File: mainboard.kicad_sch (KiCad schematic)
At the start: 39 parts, among them J1 DRV8833-1, J10 Conn_02x04_Counter_Clockwise, J11 Conn_02x04_Counter_Clockwise, J12 Conn_02x04_Counter_Clockwise, J2 DRV8833-0, J3 Conn_01x02, J4 Screw_Terminal_01x06, J5 Screw_Terminal_01x06, J6 VIM4_HEADER, J7 Conn_01x02, J8 Conn_01x02, J9 Conn_02x04_Counter_Clockwise, Q1 2N7000, Q2 2N7000, SW1 RotaryEncoder_Switch, U1 MCP23017_SP

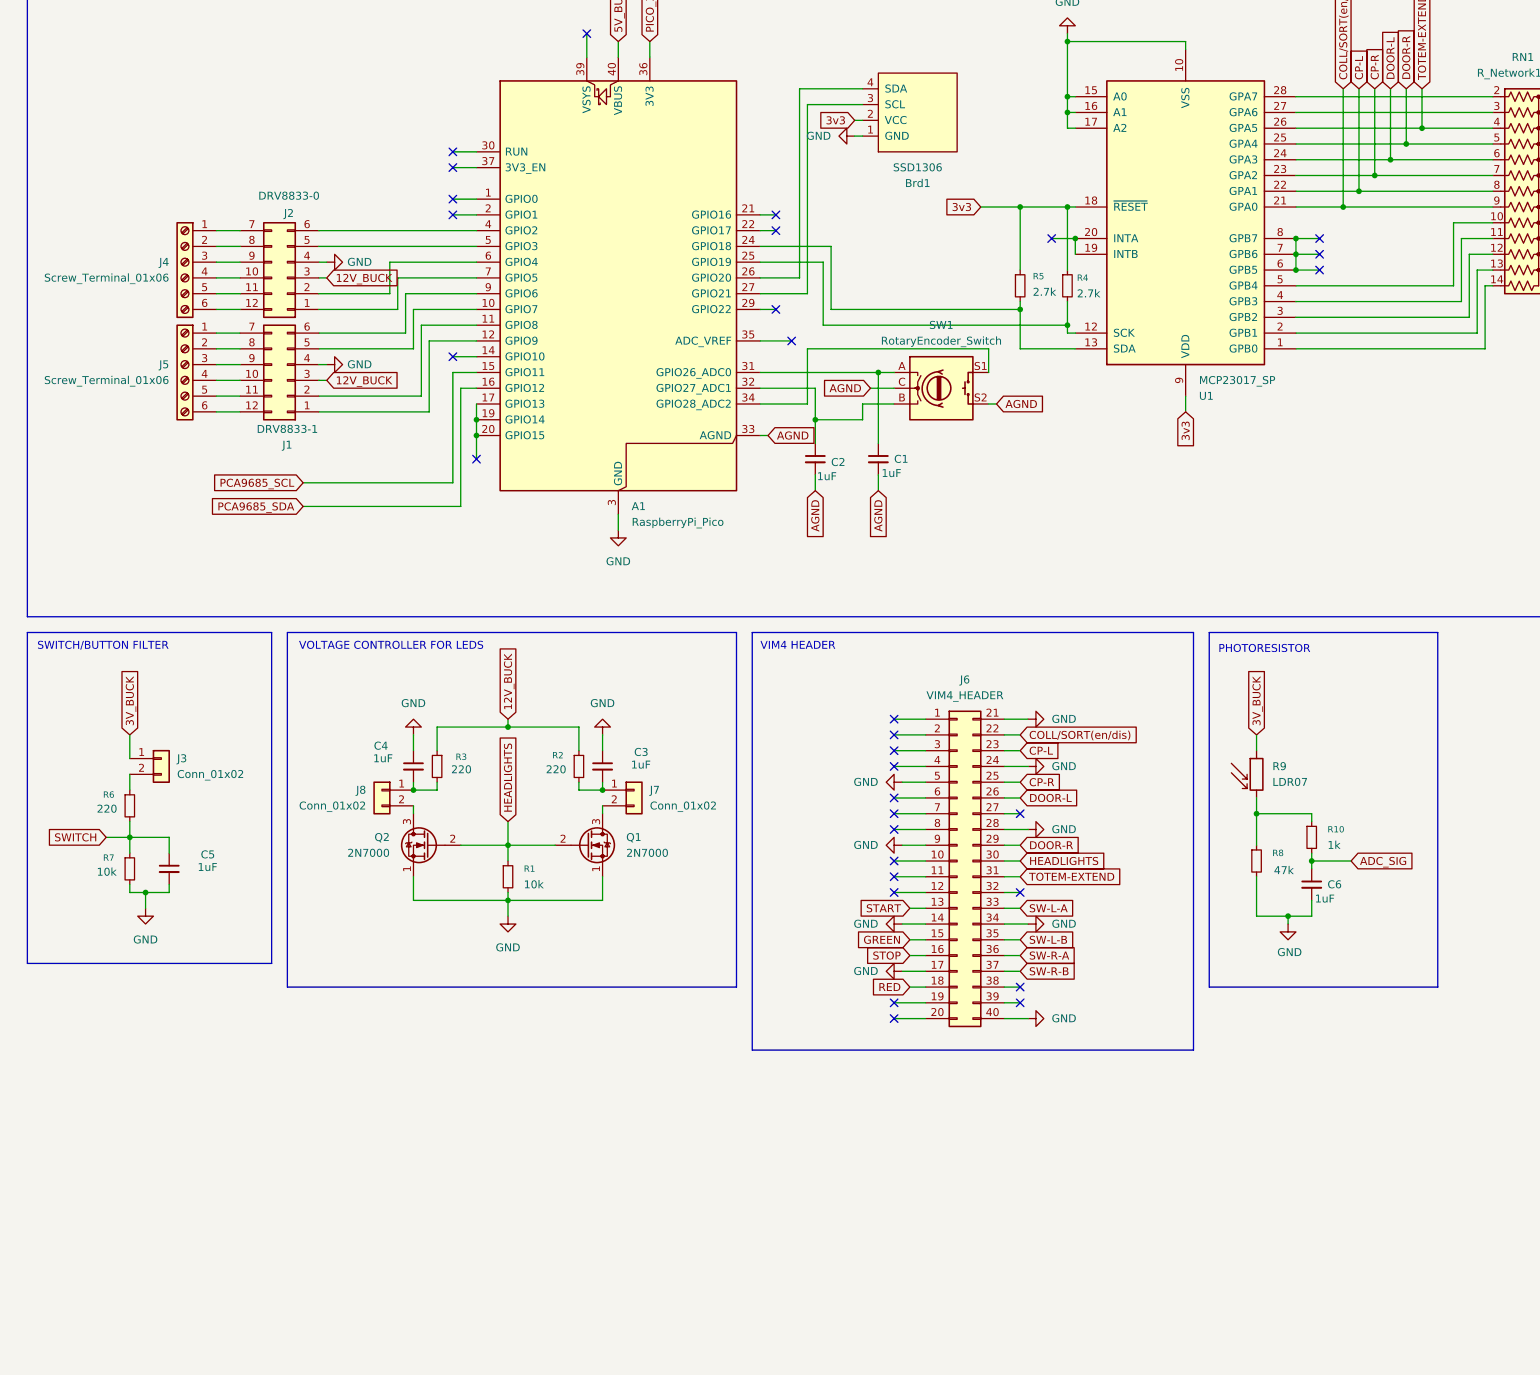
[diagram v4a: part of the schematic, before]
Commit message: Circuit adjustments / PCB component Grouping
Removed resistor on LDR in schem. Changed to 10k resistor. Added hole distance for PCA9685, SSD1309.  Grouped components.  Awaiting PIC_FOR_ADC from Dustin
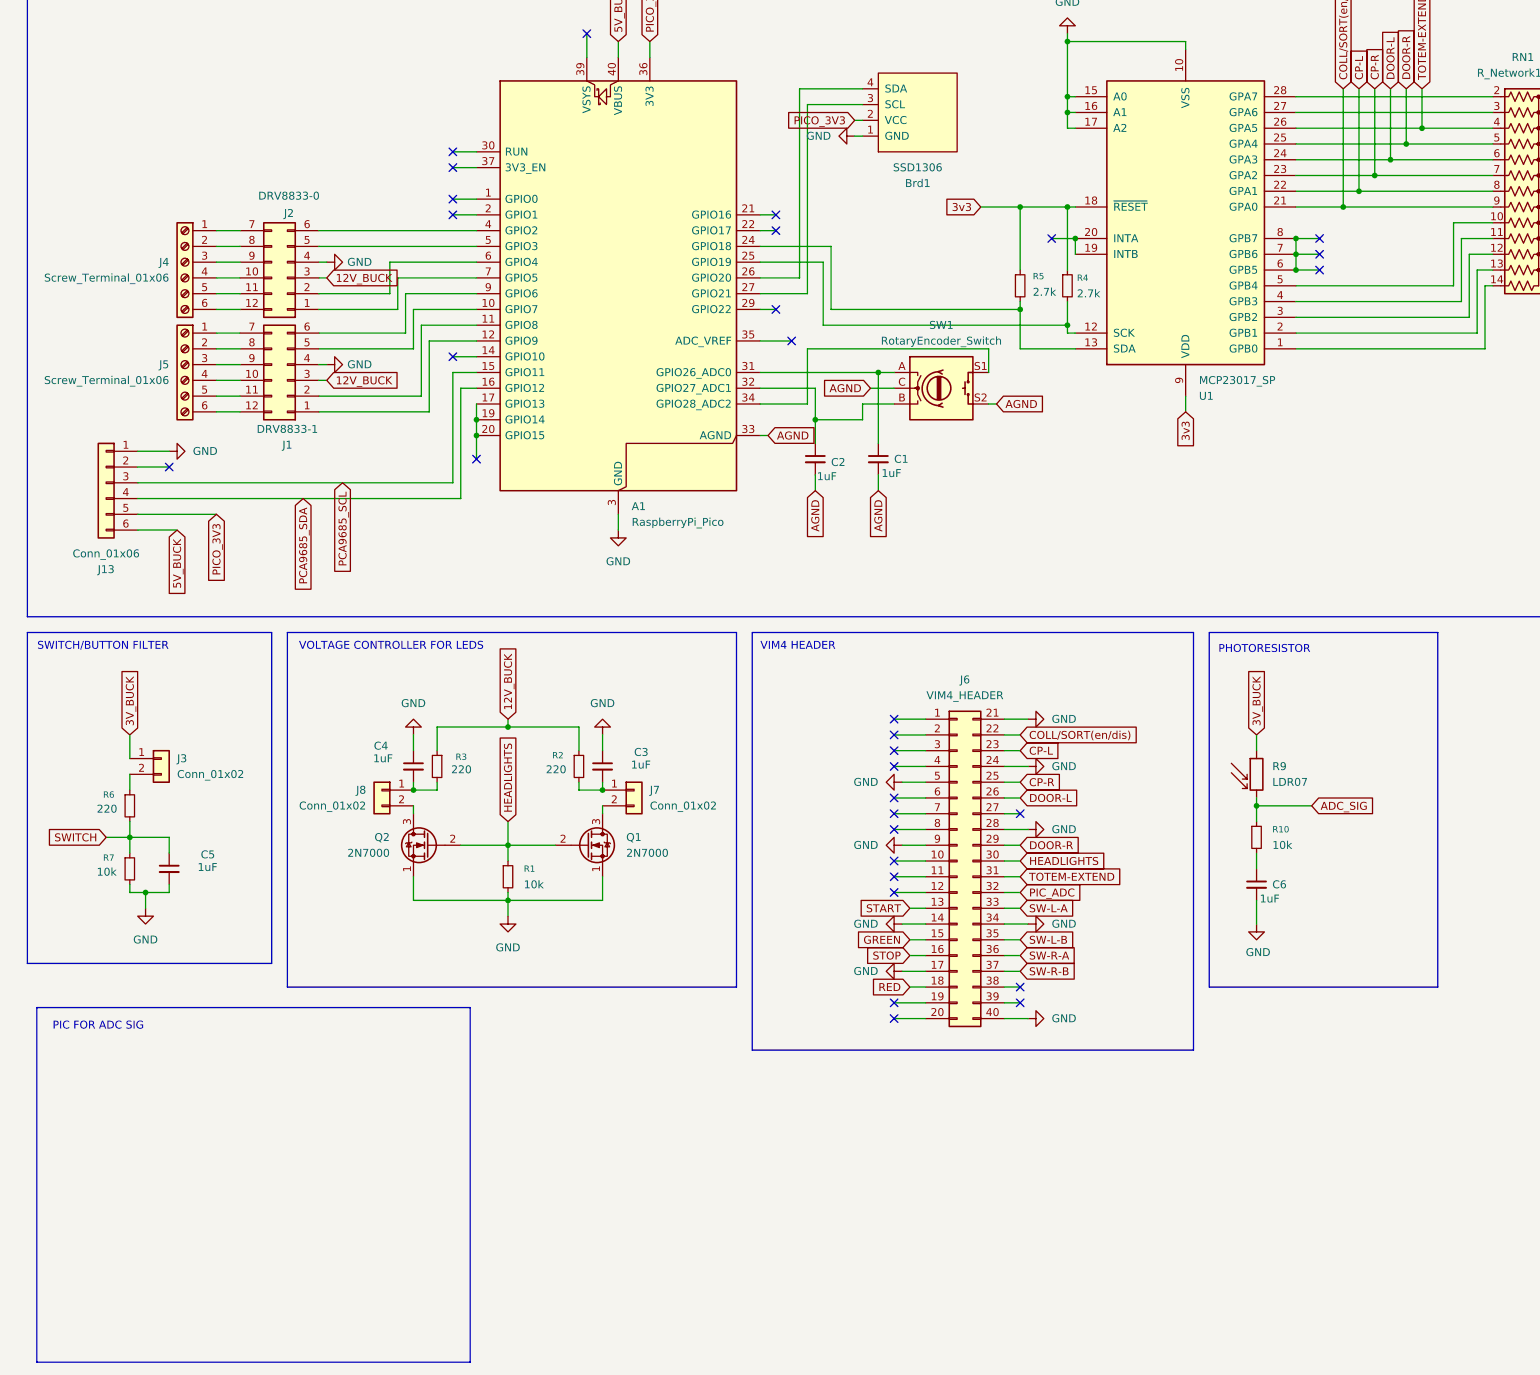
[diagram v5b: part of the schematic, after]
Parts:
- removed R8: 47k, Resistor_SMD:R_0805_2012Metric, symbol Device:R_Small
- added J13: Conn_01x06, Connector_JST:JST_EH_B6B-EH-A_1x06_P2.50mm_Vertical, symbol Connector_Generic:Conn_01x06
- R10: value 1k -> 10k
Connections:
- net 3v3: no longer Brd1.2 (VCC)
- net 5V_BUCK: now also J13.6 (Pin_6)
- net ADC_SIG: now also R10.1, R9.2; no longer C6.1, R10.2
- net GND: now also J13.1 (Pin_1)
- net PCA9685_SCL: now also J13.3 (Pin_3)
- net PCA9685_SDA: now also J13.4 (Pin_4)
- net PICO_3V3: now also Brd1.2 (VCC), J13.5 (Pin_5)
- net PIC_ADC: now reaches J6.32 (Pin_32)
- new net: C6.1, R10.2
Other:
- note added: "PIC FOR ADC SIG"
- moved on the sheet: C6, R10

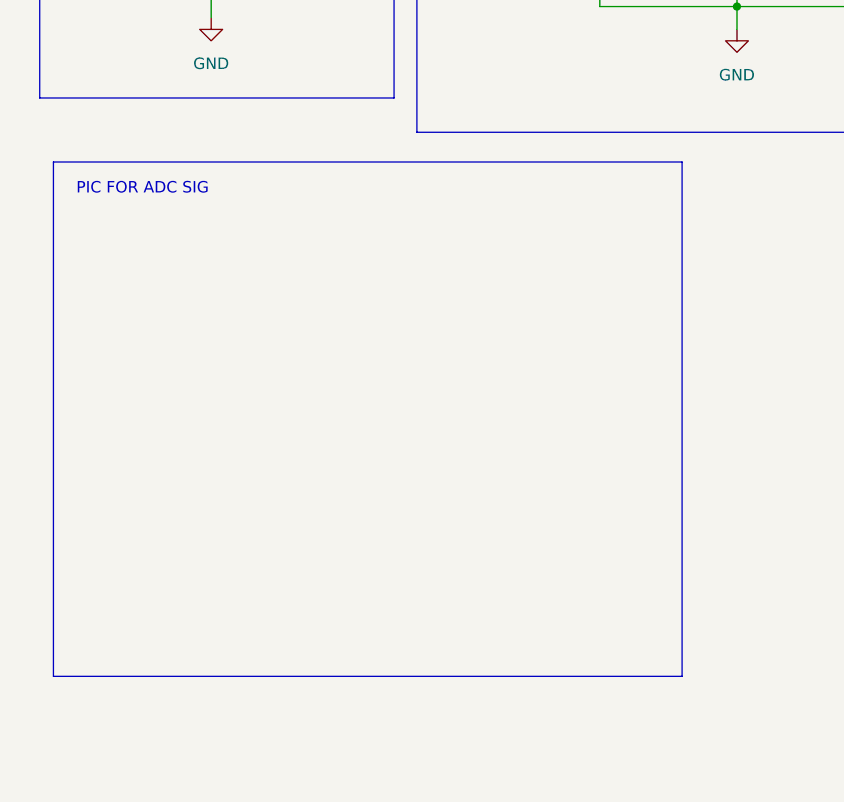
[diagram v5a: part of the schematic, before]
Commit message: PIC16F819-ISO Added
Added PIC, changed footprint to match our 18pin SMD.

LDR circuit and connection to VIM4 need to be made
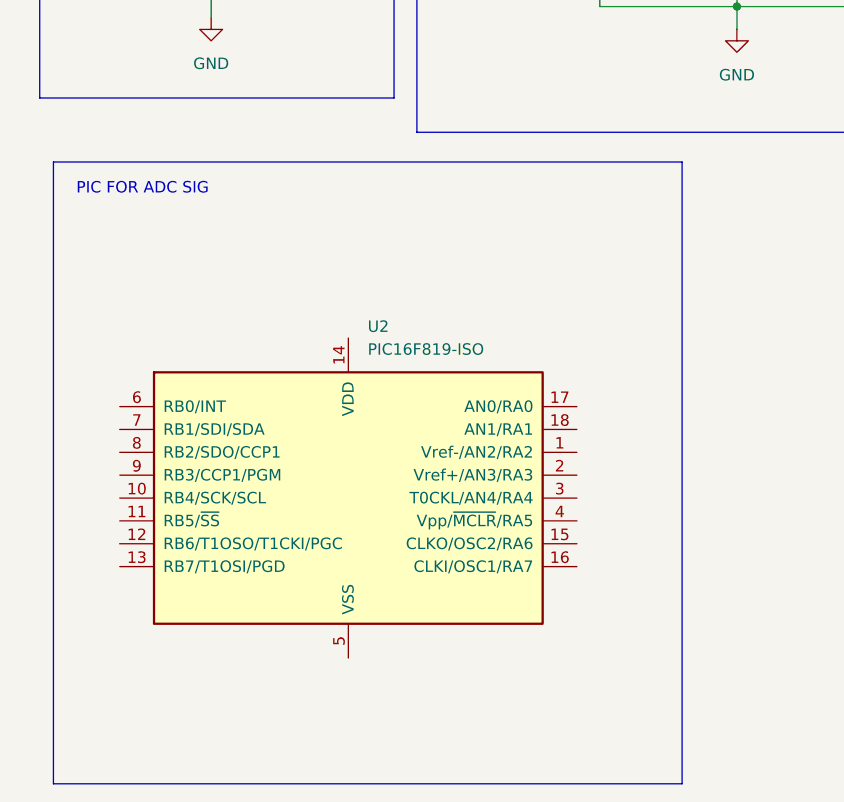
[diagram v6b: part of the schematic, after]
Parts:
- added U2: PIC16F819-ISO, Package_SO:SOIC-18W_7.5x11.6mm_P1.27mm, symbol MCU_Microchip_PIC16:PIC16F819-ISO
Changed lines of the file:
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@@
 	(rectangle
 		(start 14.224 188.722)
-		(end 84.074 245.872)
+		(end 84.074 257.81)
 		(stroke
 			(width 0)
@@
 					(unit 1)
 				)
+			)
+		)
+	)
+	(symbol
+		(lib_id "MCU_Microchip_PIC16:PIC16F819-ISO")
+		(at 46.99 226.06 0)
+		(unit 1)
+		(exclude_from_sim no)
+		(in_bom yes)
+		(on_board yes)
+		(dnp no)
+		(fields_autoplaced yes)
+		(property "Reference" "U2"
+			(at 49.1333 207.01 0)
+			(effects
+				(font
+					(size 1.27 1.27)
+				)
+				(justify left)
+			)
+		)
+		(property "Value" "PIC16F819-ISO"
+			(at 49.1333 209.55 0)
+			(effects
+				(font
+					(size 1.27 1.27)
+				)
+				(justify left)
+			)
+		)
+		(property "Footprint" "Package_SO:SOIC-18W_7.5x11.6mm_P1.27mm"
+			(at 46.99 226.06 0)
+			(effects
+				(font
+					(size 1.27 1.27)
+					(italic yes)
+				)
+				(hide yes)
+			)
+		)
+		(property "Datasheet" "http://ww1.microchip.com/downloads/en/DeviceDoc/39598F.pdf"
+			(at 46.99 226.06 0)
+			(effects
+				(font
+					(size 1.27 1.27)
+				)
+				(hide yes)
+			)
+		)
+		(property "Description" "PIC16F819, 3584B Flash, 256B SRAM, 256B EEPROM, ADC, SOIC18"
+			(at 46.99 226.06 0)
+			(effects
+				(font
+					(size 1.27 1.27)
+				)
+				(hide yes)
+			)
+		)
+		(pin "7"
+		)
+		(pin "8"
+		)
+		(pin "11"
+		)
+		(pin "6"
+		)
+		(pin "15"
+		)
+		(pin "9"
+		)
+		(pin "13"
+		)
+		(pin "17"
+		)
+		(pin "2"
+		)
+		(pin "3"
+		)
+		(pin "12"
+		)
+		(pin "14"
+		)
+		(pin "10"
+		)
+		(pin "5"
+		)
+		(pin "18"
+		)
+		(pin "1"
+		)
+		(pin "4"
+		)
+		(pin "16"
+		)
+		(instances
+			(project ""
+				(path "/c17272df-bb38-44d5-9de0-abe2e6f0941d"
+					(reference "U2")
+					(unit 1)
+				)

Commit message: Rearrangement and first pour
Modified the order of operations for terminal block to fuse to buck. Added a few things like the holes for the Roboclaws, removed the display, since we're going to wire it using a JST connector in order for it to exist somewhere else on the robot.  I added a PIC footprint that fits the PIC16F819-ISO, and generally hooked it up.

I still need to check with Dustin and make sure that the VIM4 connection to the PIC is the one we want to use.

I also need to know the exact dimensions of the PCB constraint we are designing this for.
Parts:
- added C7: 0.1uF, Capacitor_SMD:C_0805_2012Metric, symbol Device:C_Small
- added D1: LED_Small, symbol Device:LED_Small
- added R8: 10k, Resistor_SMD:R_0805_2012Metric, symbol Device:R_Small
- added SW3: SW_SPST, symbol Switch:SW_SPST
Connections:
- net ADC_SIG is gone; now on net LDR_ADC: R10.1, R9.2
- net PIC_ADC is gone; now on net PIC_STATE: J6.32 (Pin_32)
- net 12V_BUCK: now also J12.7 (Pin_7), J12.8 (Pin_8); no longer F2.2
- net 3V_BUCK: now also J9.7 (Pin_7), J9.8 (Pin_8), U2.14 (VDD), C7.2, R8.1; no longer F4.2
- net 5V_BUCK: now also J10.7 (Pin_7), J10.8 (Pin_8); no longer F3.2
- net 9V_BUCK: now also J11.7 (Pin_7), J11.8 (Pin_8); no longer F1.2
- net GND: now also U2.5 (VSS), C7.1, D1.1 (K)
- net LDR_ADC: now reaches U2.17 (AN0/RA0)
- net PIC_STATE: now reaches U2.3 (T0CKL/AN4/RA4)
- net at U2.4 (Vpp/~{MCLR}/RA5): now also R8.2
- removed net MAINS: J10.1 (Pin_1), J10.2 (Pin_2), J11.1 (Pin_1), J11.2 (Pin_2), J12.1 (Pin_1), J12.2 (Pin_2), J9.1 (Pin_1), J9.2 (Pin_2)
- new net: F2.2, J12.1 (Pin_1), J12.2 (Pin_2)
- new net: F4.2, J9.1 (Pin_1), J9.2 (Pin_2)
- new net: F3.2, J10.1 (Pin_1), J10.2 (Pin_2)
- new net: F1.2, J11.1 (Pin_1), J11.2 (Pin_2)
- new net BATTERY: SW3.1 (A)
- new net MAIN_BUS: D1.2 (A), F1.1, F2.1, F3.1, F4.1, SW3.2 (B)
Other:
- note added: "MAIN ON/OFF - EMERGENCY SWITCH"
- moved on the sheet: F1, F2, F3, F4, J10, J11, J12, J9, U2

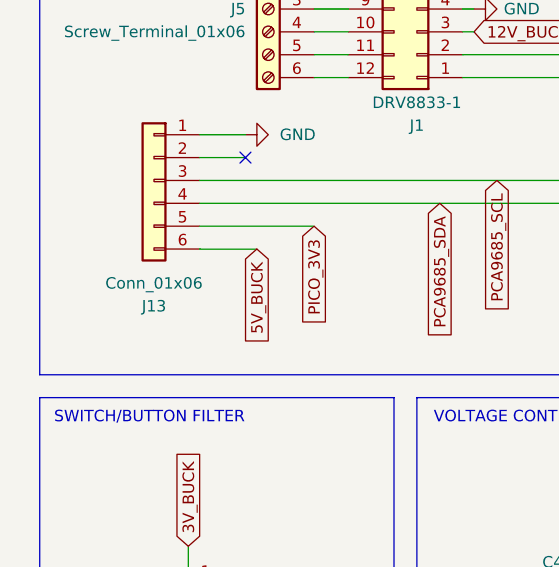
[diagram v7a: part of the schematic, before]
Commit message: Peripheral footprint blanks and boundaries
Peripheral footprint blanks and boundaries added
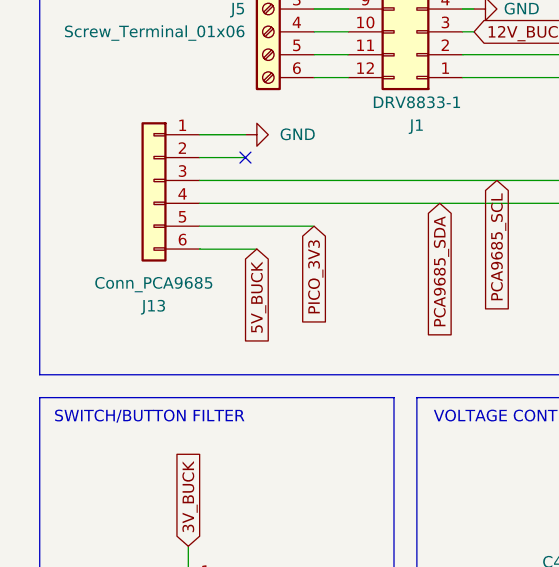
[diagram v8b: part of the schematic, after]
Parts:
- J13: value Conn_01x06 -> Conn_PCA9685
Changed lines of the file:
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@@
 			)
 		)
-		(property "Value" "Conn_01x06"
+		(property "Value" "Conn_PCA9685"
 			(at 25.4 115.57 0)
 			(effects
